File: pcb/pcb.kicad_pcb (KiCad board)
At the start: 2 copper layers, 157 x 88.8 mm, 122 parts, among them J301 USB_C_Receptacle_USB2.0_16P, J302 JTAG, J501 UART, Q201 IRL540N, Q301 Q_Dual_PMOS_S1G1S2G2D2D2D1D1, SW501 Reset, SW502 Boot, T201 DA2032-AL, U1 K155ID1, U2 K155ID1, U201 LM5155, U3 K155ID1, U301 CYPD3176, U4 K155ID1, U401 AP63205WU, U411 AP63203WU, U501 ESP32-S3-WROOM-1

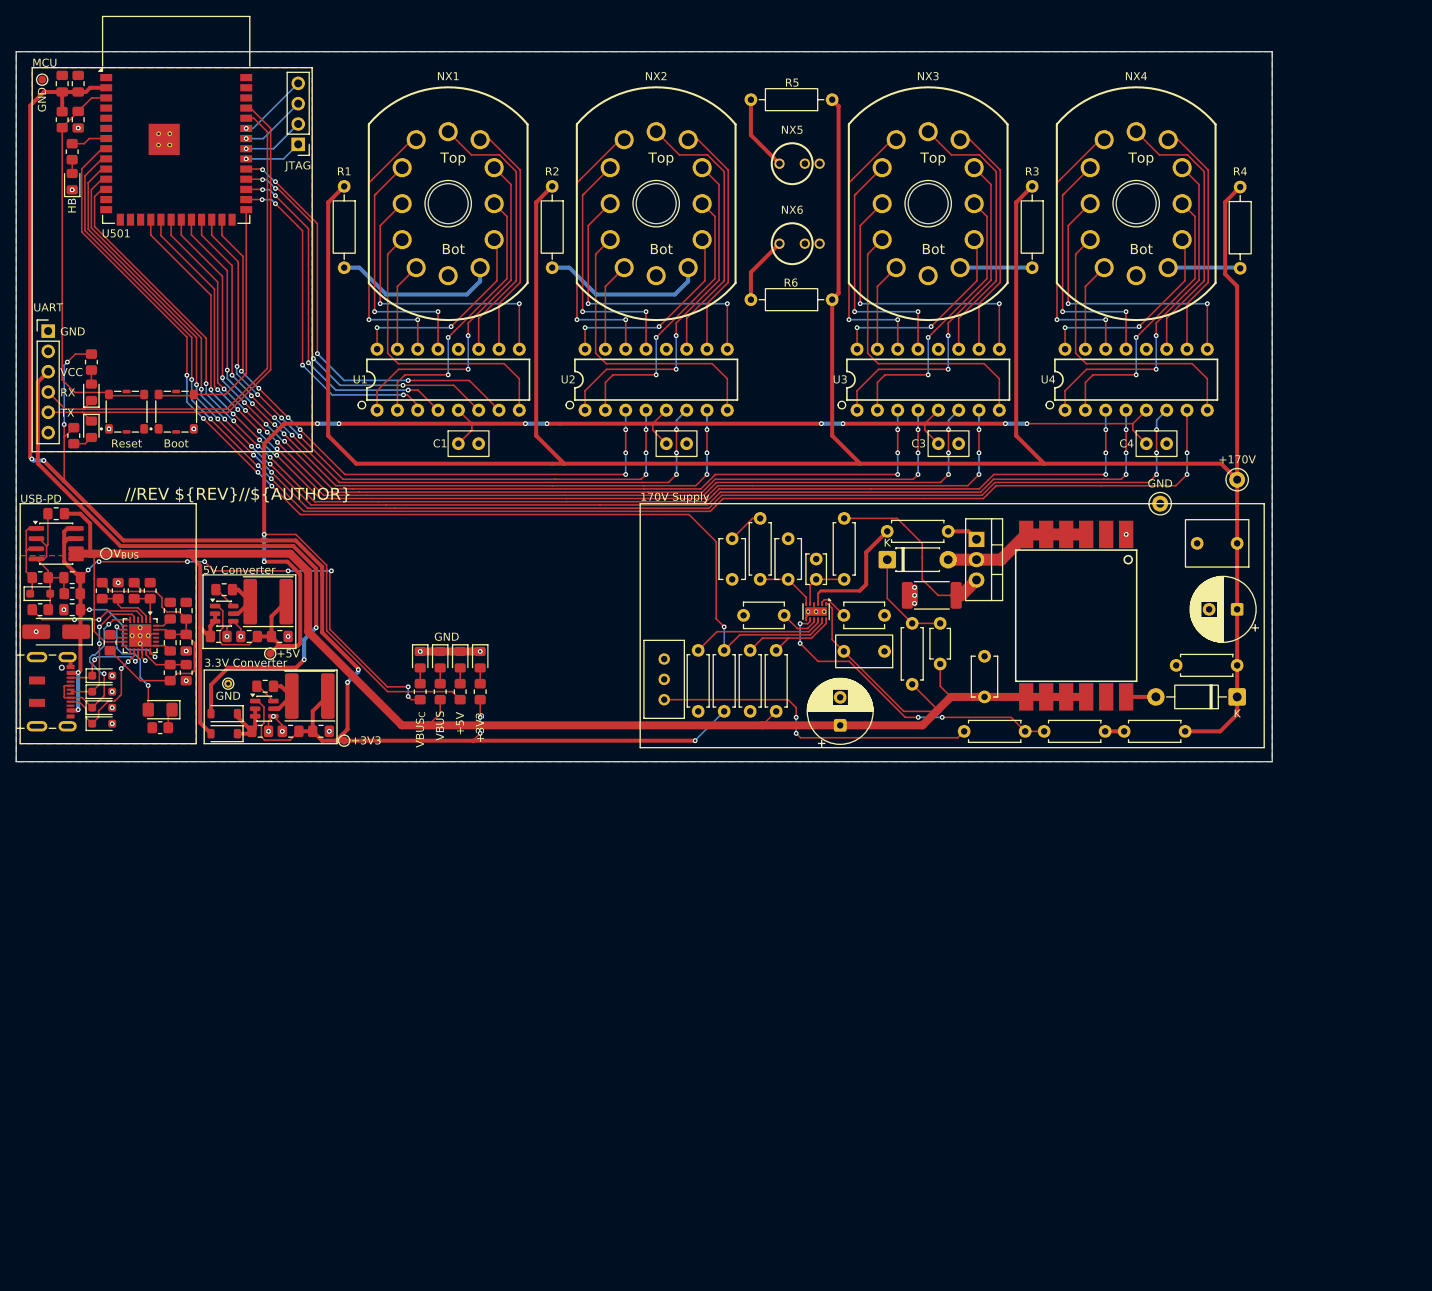
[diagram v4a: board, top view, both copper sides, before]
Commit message: Partial Rev B, committing before splitting projects
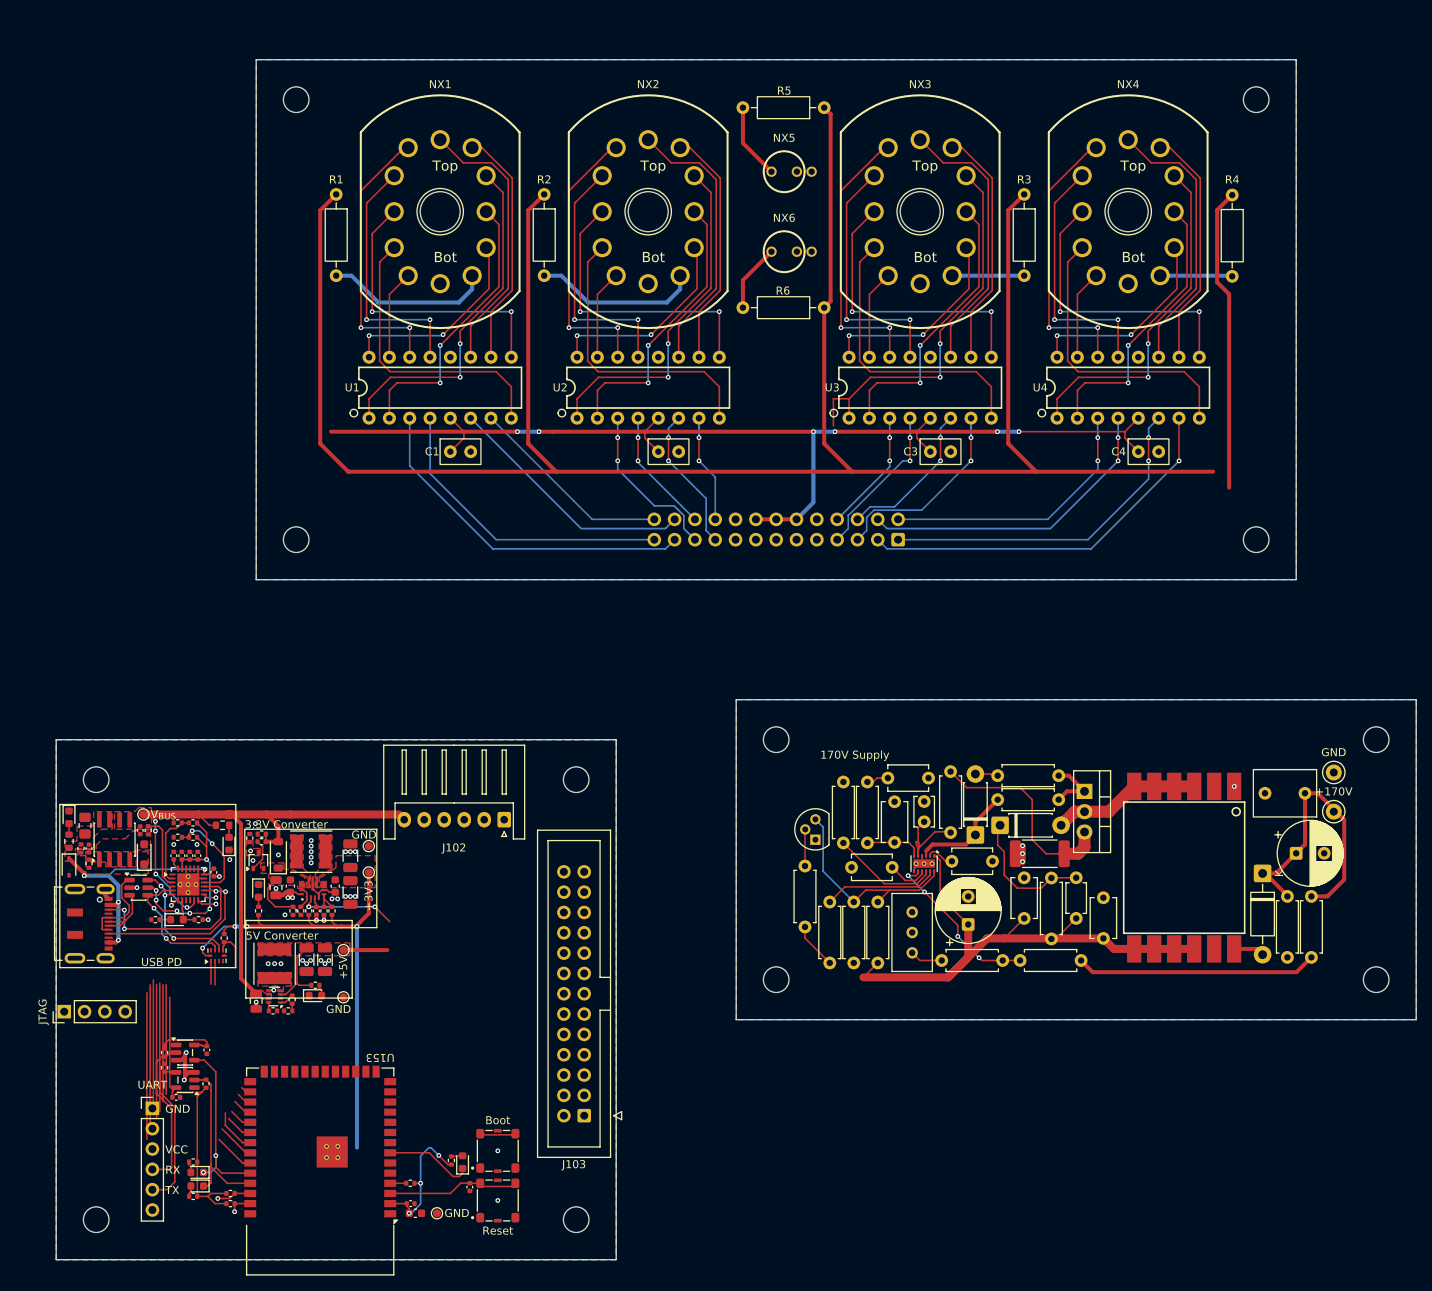
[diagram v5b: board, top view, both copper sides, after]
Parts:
- removed C211: 1uF, nixie_clock:C_Rect_L7.1mm_W4.1mm_P5.08mm_Goldmax
- removed C302, C303, C306, C503: 1uF, Capacitor_SMD:C_0805_2012Metric_Pad1.18x1.45mm_HandSolder
- removed C307, C402, C412: 100nF, Capacitor_SMD:C_0805_2012Metric_Pad1.18x1.45mm_HandSolder
- removed C401, C411: 10uF, Capacitor_SMD:C_0805_2012Metric_Pad1.18x1.45mm_HandSolder
- removed C403, C404, C413, C414: 22uF, Capacitor_SMD:C_0805_2012Metric_Pad1.18x1.45mm_HandSolder
- removed D301: VBUS_{C}, LED_SMD:LED_0805_2012Metric_Pad1.15x1.40mm_HandSolder
- removed D302, D303: ESDA051, Diode_SMD:D_SOD-323_HandSoldering
- removed D304, D306: ESDA051-1JY, Diode_SMD:D_SOD-323_HandSoldering
- removed D309: VBUS, LED_SMD:LED_0805_2012Metric_Pad1.15x1.40mm_HandSolder
- removed D310: HB, LED_SMD:LED_0805_2012Metric_Pad1.15x1.40mm_HandSolder
- removed D401: +5V, LED_SMD:LED_0805_2012Metric_Pad1.15x1.40mm_HandSolder
- removed D411, D412: D_Schottky, Diode_SMD:D_SOD-123
- removed D413: +3V3, LED_SMD:LED_0805_2012Metric_Pad1.15x1.40mm_HandSolder
- removed D501: TX, LED_SMD:LED_0805_2012Metric_Pad1.15x1.40mm_HandSolder
- removed D502: RX, LED_SMD:LED_0805_2012Metric_Pad1.15x1.40mm_HandSolder
- removed L401, L411: 4.7uH, Inductor_SMD:L_APV_ANR6045
- removed R301, R303, R307, R309, R401: 5.1k, Resistor_SMD:R_0805_2012Metric_Pad1.20x1.40mm_HandSolder
- removed R302, R312, R501: 10k, Resistor_SMD:R_0805_2012Metric_Pad1.20x1.40mm_HandSolder
- removed R304, R306, R310, R313: 1k, Resistor_SMD:R_0805_2012Metric_Pad1.20x1.40mm_HandSolder
- removed R314, R411, R502, R503: 1.5k, Resistor_SMD:R_0805_2012Metric_Pad1.20x1.40mm_HandSolder
- removed TP401: +5V, TestPoint:TestPoint_Pad_D1.0mm
- removed TP402: GND, TestPoint:TestPoint_THTPad_D1.0mm_Drill0.5mm
- removed TP411: +3V3, TestPoint:TestPoint_Pad_D1.0mm
- removed U401: AP63205WU, Package_TO_SOT_SMD:TSOT-23-6
- removed U411: AP63203WU, Package_TO_SOT_SMD:TSOT-23-6
- added C102: 100nF, Capacitor_SMD:C_0402_1005Metric, F.Cu at (49.7, 141.6)
- added C103: 1uF, Capacitor_SMD:C_0402_1005Metric, F.Cu at (44.7, 139.5)
- added C104: 1uF, Capacitor_SMD:C_0402_1005Metric, F.Cu at (34.1, 138.6)
- added C107: 1uF, Capacitor_SMD:C_0402_1005Metric, F.Cu at (40.5, 136.3)
- added C108: 100nF, Capacitor_SMD:C_0402_1005Metric, F.Cu at (47.7, 139.5)
- added C109: 10nF, nixie_clock:C_Rect_L5.1mm_W3.2mm_P5.08mm_Goldmax, F.Cu at (151.0, 144.8)
- added C121: 10uF, Capacitor_SMD:C_0805_2012Metric, F.Cu at (57.5, 143.5)
- added C122: 10uF, Capacitor_SMD:C_0603_1608Metric, F.Cu at (59.3, 143.3)
- added C123: 100nF, Capacitor_SMD:C_0402_1005Metric, F.Cu at (62.5, 146.4)
- added C124: 10uF, Capacitor_SMD:C_0603_1608Metric, F.Cu at (64.9, 143.3)
- added C125: 22uF, Capacitor_SMD:C_1206_3216Metric, F.Cu at (66.8, 144.1)
- added C126: 47uF, Capacitor_SMD:C_1206_3216Metric, F.Cu at (66.8, 139.5)
- added C131: 10uF, Capacitor_SMD:C_0805_2012Metric, F.Cu at (55.0, 157.7)
- added C132: 22uF, Capacitor_SMD:C_1206_3216Metric, F.Cu at (61.3, 152.5)
- added C133: 22uF, Capacitor_SMD:C_1206_3216Metric, F.Cu at (63.6, 152.5)
- added C151: 100nF, Capacitor_SMD:C_0402_1005Metric, F.Cu at (45.0, 169.7)
- added C152: 100nF, Capacitor_SMD:C_0402_1005Metric, F.Cu at (48.8, 163.8)
- added C153: 100nF, Capacitor_SMD:C_0402_1005Metric, F.Cu at (81.7, 180.9)
- added D1: SB240S, Diode_THT:D_DO-41_SOD81_P7.62mm_Horizontal, F.Cu at (144.9, 136.9)
- added D101: V_{BUSC}, LED_SMD:LED_0603_1608Metric, F.Cu at (31.6, 134.7)
- added D105: V_{BUS}, LED_SMD:LED_0603_1608Metric, F.Cu at (51.6, 138.0)
- added D121: 1N5819, Diode_SMD:D_SOD-123, F.Cu at (57.8, 139.4)
- added D122: +3.3V, LED_SMD:LED_0603_1608Metric, F.Cu at (55.3, 143.9)
- added D131: +5V, LED_SMD:LED_0603_1608Metric, F.Cu at (62.4, 157.0)
- added D151: TX, LED_SMD:LED_0603_1608Metric, F.Cu at (47.6, 180.8)
- added D152: RX, LED_SMD:LED_0603_1608Metric, F.Cu at (47.6, 179.1)
- added D153: HB, LED_SMD:LED_0603_1608Metric, F.Cu at (80.8, 177.8)
- added H101: MountingHole, MountingHole:MountingHole_3.2mm_M3_ISO7380, F.Cu at (35.0, 130.0)
- added H102: MountingHole, MountingHole:MountingHole_3.2mm_M3_ISO7380, F.Cu at (95.0, 130.0)
- added H103: MountingHole, MountingHole:MountingHole_3.2mm_M3_ISO7380, F.Cu at (35.0, 185.0)
- added H104: MountingHole, MountingHole:MountingHole_3.2mm_M3_ISO7380, F.Cu at (95.0, 185.0)
- added H2: MountingHole, MountingHole:MountingHole_3.2mm_M3_ISO7380, F.Cu at (60.0, 45.0)
- added H3: MountingHole, MountingHole:MountingHole_3.2mm_M3_ISO7380, F.Cu at (180.0, 45.0)
- added H4: MountingHole, MountingHole:MountingHole_3.2mm_M3_ISO7380, F.Cu at (60.0, 100.0)
- added H5: MountingHole, MountingHole:MountingHole_3.2mm_M3_ISO7380, F.Cu at (180.0, 100.0)
- added H6: MountingHole, MountingHole:MountingHole_3.2mm_M3_ISO7380, F.Cu at (120.0, 125.0)
- added H7: MountingHole, MountingHole:MountingHole_3.2mm_M3_ISO7380, F.Cu at (195.0, 125.0)
- added H8: MountingHole, MountingHole:MountingHole_3.2mm_M3_ISO7380, F.Cu at (120.0, 155.0)
- added H9: MountingHole, MountingHole:MountingHole_3.2mm_M3_ISO7380, F.Cu at (195.0, 155.0)
- added J102: Conn_01x06, Connector_JST:JST_XH_S6B-XH-A_1x06_P2.50mm_Horizontal, F.Cu at (86.0, 135.0)
- added J103: Conn_02x13_Counter_Clockwise, Connector_IDC:IDC-Header_2x13_P2.54mm_Vertical, F.Cu at (96.0, 172.0)
- added J104: Conn_02x13_Counter_Clockwise, Connector_IDC:IDC-Header_2x13_P2.54mm_Vertical, B.Cu at (135.2, 100.0)
- added L121: 1.5uH, nixie_clock:L_Bourns_SRN5040TA, F.Cu at (61.9, 139.0)
- added L131: 2.2uH, nixie_clock:L_Bourns_SRN5040TA, F.Cu at (57.3, 153.0)
- added Q121: PMF170XP, Package_TO_SOT_SMD:SOT-323_SC-70, F.Cu at (55.3, 140.1)
- added Q151: TN2106N3-G, Package_TO_SOT_THT:TO-92L, F.Cu at (124.9, 137.5)
- added R101: 5.1k, Resistor_SMD:R_0603_1608Metric, F.Cu at (31.6, 137.7)
- added R102: 10k, Resistor_SMD:R_0402_1005Metric, F.Cu at (51.0, 149.8)
- added R103: 10k, Resistor_SMD:R_0402_1005Metric, F.Cu at (33.1, 138.6)
- added R105: 1k, Resistor_SMD:R_0402_1005Metric, F.Cu at (41.5, 136.3)
- added R106: 5.1k, Resistor_SMD:R_0402_1005Metric, F.Cu at (47.1, 137.2)
- added R107: 2.4k, Resistor_SMD:R_0402_1005Metric, F.Cu at (45.2, 137.2)
- added R108: 5.1k, Resistor_SMD:R_0402_1005Metric, F.Cu at (47.1, 135.4)
- added R111: 5.1k, Resistor_SMD:R_0603_1608Metric, F.Cu at (50.8, 135.7)
- added R112: 100k, Resistor_SMD:R_0402_1005Metric, F.Cu at (47.8, 147.5)
- added R113: 10k, Resistor_SMD:R_0402_1005Metric, F.Cu at (55.7, 136.8)
- added R121: 10k, Resistor_SMD:R_0402_1005Metric, F.Cu at (59.6, 146.4)
- added R122: 100k, Resistor_SMD:R_0402_1005Metric, F.Cu at (55.7, 137.8)
- added R123: 100k, Resistor_SMD:R_0402_1005Metric, F.Cu at (54.2, 137.3)
- added R124: 10k, Resistor_SMD:R_0402_1005Metric, F.Cu at (60.6, 146.4)
- added R125: 120k, Resistor_SMD:R_0402_1005Metric, F.Cu at (64.5, 146.4)
- added R126: 39k, Resistor_SMD:R_0402_1005Metric, F.Cu at (63.5, 146.4)
- added R127: 100k, Resistor_SMD:R_0402_1005Metric, F.Cu at (61.6, 146.4)
- added R128: 1k, Resistor_SMD:R_0402_1005Metric, F.Cu at (55.3, 146.4)
- added R13: 3.3, Resistor_THT:R_Axial_DIN0207_L6.3mm_D2.5mm_P7.62mm_Horizontal, F.Cu at (147.7, 129.5)
- added R131: 27k, Resistor_SMD:R_0402_1005Metric, F.Cu at (57.1, 158.9)
- added R132: 75k, Resistor_SMD:R_0402_1005Metric, F.Cu at (59.5, 157.5)
- added R133: 5.6k, Resistor_SMD:R_0402_1005Metric, F.Cu at (59.0, 158.9)
- added R134: 2.2k, Resistor_SMD:R_0402_1005Metric, F.Cu at (62.4, 155.7)
- added R151: 150, Resistor_SMD:R_0402_1005Metric, F.Cu at (43.6, 166.0)
- added R152: 10k, Resistor_SMD:R_0402_1005Metric, F.Cu at (43.6, 164.1)
- added R153: 680, Resistor_SMD:R_0402_1005Metric, F.Cu at (47.1, 182.1)
- added R154: 680, Resistor_SMD:R_0402_1005Metric, F.Cu at (47.1, 177.8)
- added R155: 10k, Resistor_SMD:R_0402_1005Metric, F.Cu at (48.7, 168.0)
- added R156: 10k, Resistor_SMD:R_0402_1005Metric, F.Cu at (51.8, 183.0)
- added R157: 680, Resistor_SMD:R_0402_1005Metric, F.Cu at (79.4, 177.6)
- added R158: 10k, Resistor_SMD:R_0402_1005Metric, F.Cu at (51.8, 181.7)
- added R159: 10k, Resistor_SMD:R_0402_1005Metric, F.Cu at (74.3, 180.4)
- added R160: 100k, Resistor_THT:R_Axial_DIN0207_L6.3mm_D2.5mm_P7.62mm_Horizontal, F.Cu at (123.6, 148.4)
- added TP121: +3V3, TestPoint:TestPoint_Pad_D1.0mm, F.Cu at (69.1, 141.6)
- added TP122: GND, TestPoint:TestPoint_Pad_D1.0mm, F.Cu at (69.1, 138.3)
- added TP131: +5V, TestPoint:TestPoint_Pad_D1.0mm, F.Cu at (65.9, 151.3)
- added TP132: GND, TestPoint:TestPoint_Pad_D1.0mm, F.Cu at (65.9, 157.2)
- added U101: USBLC6-2SC6, Package_TO_SOT_SMD:SOT-23-6, F.Cu at (40.3, 143.5)
- added U102: TS3USB221A, nixie_clock:UQFN-10_1.5x2mm_P0.5mm_TI_RSE0010A, F.Cu at (50.1, 152.0)
- added U121: TPS63070, nixie_clock:VQFN-15_2.5x3mm_TI_RNM0015A, F.Cu at (62.1, 143.6)
- added U131: TPS629203, Package_TO_SOT_SMD:SOT-583-8, F.Cu at (57.3, 157.1)
- added U151: 74LVC1G17, Package_TO_SOT_SMD:SOT-23-5, F.Cu at (46.1, 167.5)
- added U152: 74LVC1G17, Package_TO_SOT_SMD:SOT-23-5, F.Cu at (46.1, 164.1)
- C105: renamed from C304; footprint Capacitor_SMD:C_0805_2012Metric_Pad1.18x1.45mm_HandSolder -> Capacitor_SMD:C_0402_1005Metric
- C106: renamed from C305; footprint Capacitor_SMD:C_0805_2012Metric_Pad1.18x1.45mm_HandSolder -> Capacitor_SMD:C_0402_1005Metric
- C13: renamed from C209; value 10nF -> 12nF
- C154: renamed from C502; footprint Capacitor_SMD:C_0805_2012Metric_Pad1.18x1.45mm_HandSolder -> Capacitor_SMD:C_0603_1608Metric
- C155: renamed from C501; footprint Capacitor_SMD:C_0805_2012Metric_Pad1.18x1.45mm_HandSolder -> Capacitor_SMD:C_0402_1005Metric
- C9: renamed from C206; value 47nF -> 220nF
- D102: renamed from D305; value SMAJ15A -> SD15Q-7; footprint Diode_SMD:D_SMA_Handsoldering -> Diode_SMD:D_SOD-323
- D104: renamed from D308; footprint LED_SMD:LED_1206_3216Metric_Pad1.42x1.75mm_HandSolder -> LED_SMD:LED_0603_1608Metric
- R104: renamed from R305; footprint Resistor_SMD:R_0805_2012Metric_Pad1.20x1.40mm_HandSolder -> Resistor_SMD:R_0402_1005Metric
- R109: renamed from R308; footprint Resistor_SMD:R_0805_2012Metric_Pad1.20x1.40mm_HandSolder -> Resistor_SMD:R_0402_1005Metric
- R110: renamed from R311; value 220 -> 1k; footprint Resistor_SMD:R_0805_2012Metric_Pad1.20x1.40mm_HandSolder -> Resistor_SMD:R_0402_1005Metric
- R12: renamed from R212; value 27k -> 30k
- R20: renamed from R202; value 470k -> 1.5M
- U5: renamed from U201; footprint Package_SON:WSON-12-1EP_3x2mm_P0.5mm_EP1x2.65_ThermalVias -> nixie_clock:WSON-12-1EP_3x2mm_P0.5mm_EP1x2.65_ThermalVias
- moved TP151 150.0 mm to (77.6, 184.2), turned to 90 degrees
- moved C154 147.9 mm to (74.9, 184.2), turned to 0 degrees
- moved C155 146.0 mm to (74.3, 183.0), turned to 0 degrees
- moved U153 132.7 mm to (63.0, 179.0), turned to 180 degrees
- moved J152 112.3 mm to (31.0, 159.0), turned to 90 degrees
- moved SW152 109.0 mm to (85.2, 182.6)
- moved SW151 100.8 mm to (85.2, 176.4)
- moved J151 98.0 mm to (42.0, 171.1)
- moved RV1 44.3 mm to (137.0, 151.6)
- moved TP2 43.2 mm to (189.7, 134.0)
- moved TP1 40.0 mm to (189.7, 129.1)
- moved Q101 37.7 mm to (37.3, 137.5), turned to 90 degrees
- moved R12 36.3 mm to (154.4, 149.9)
- moved R14 36.3 mm to (147.7, 132.5)
- moved R104 36.3 mm to (34.1, 140.5), turned to 90 degrees
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- renumbered C207 to C10, C301 to C101, C210 to C11, C208 to C12, C204 to C14, C205 to C15, C202 to C5, C203 to C6, C201 to C7, D307 to D103, D202 to D2, D201 to D3, J301 to J101, J501 to J151, J302 to J152, Q201 to Q1, Q301 to Q101, R209 to R10, R210 to R11, R211 to R14, R213 to R15, R201 to R16, R203 to R17, R204 to R18, R205 to R19, R206 to R7, R207 to R8, R208 to R9, RV201 to RV1, SW502 to SW151, SW501 to SW152, T201 to T1, TP202 to TP1, TP301 to TP101, TP501 to TP151, TP201 to TP2, U301 to U103, U501 to U153
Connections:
- net /HV/GATE renamed /HV/GATE_{LM5155}
- net /MCU/EN renamed EN_{MCU}
- net Net-(Q201-G) renamed /HV/GATE_{IRL540N}
- net Net-(Q201-S) renamed /HV/SOURCE_{IRL540N}
- D104 pad 2: /PWR/FAULT -> PD_{FLT}
- J101 pad A6: USB_{D+} -> /PWR/D+_{J}
- J101 pad A7: USB_{D-} -> /PWR/D-_{J}
- J101 pad B6: USB_{D+} -> /PWR/D+_{J}
- J101 pad B7: USB_{D-} -> /PWR/D-_{J}
- J151 pad 4: /MCU/RXD0 -> /MCU/RXD0_{B}
- J151 pad 5: /MCU/TXD0 -> /MCU/TXD0_{B1}
- U103 pad 1: Net-(U301-VBUS_MIN) -> GND
- U103 pad 10: Net-(U301-DATAMODE/FLIP) -> unconnected-(U103-DATAMODE/FLIP-Pad10)
- U103 pad 12: unconnected-(U301-HPI_SDA-Pad12) -> SDA
- U103 pad 13: unconnected-(U301-HPI_SCL-Pad13) -> SCL
- U103 pad 16: GND -> Net-(U103-ISNK_FINE)
- U103 pad 17: Net-(U301-ISNK_COARSE) -> GND
- U103 pad 5: USB_{D+} -> D+
- U103 pad 6: USB_{D-} -> D-
- U103 pad 7: unconnected-(U301-HPI_INT-Pad7) -> PD_{INT}
- U103 pad 8: /PWR/FAULT -> PD_{FLT}
- U153 pad 13: unconnected-(U501-USB_D--Pad13) -> USB_{D-}
- U153 pad 14: unconnected-(U501-USB_D+-Pad14) -> USB_{D+}
- U153 pad 17: unconnected-(U501-GPIO9-Pad17) -> EN_{HV}
- U153 pad 38: unconnected-(U501-GPIO2-Pad38) -> SCL
- U153 pad 39: unconnected-(U501-GPIO1-Pad39) -> SDA
- U153 pad 4: unconnected-(U501-GPIO4-Pad4) -> PD_{INT}
- U153 pad 5: unconnected-(U501-GPIO5-Pad5) -> PD_{FLT}
- U153 pad 6: unconnected-(U501-GPIO6-Pad6) -> USB_{~{OE}}
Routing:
- net M1_{C}: track 177.2 -> 48.0 mm, vias 6 -> 1
- net M1_{B}: track 171.5 -> 42.6 mm, vias 7 -> 2
- net M1_{A}: track 159.8 -> 33.9 mm, vias 7 -> 2
- net PGOOD_{LM5155}: track 140.2 -> 14.4 mm, vias 5 -> 0
- net M1_{D}: track 164.7 -> 39.4 mm, vias 7 -> 2
- net M10_{B}: track 130.8 -> 19.3 mm, vias 7 -> 2
- net M10_{C}: track 135.4 -> 24.6 mm, vias 7 -> 2
- net M10_{A}: track 121.0 -> 15.4 mm, vias 7 -> 2
- net M10_{D}: track 124.9 -> 19.5 mm, vias 7 -> 2
- net +3V3: track 220.6 -> 123.8 mm, vias 9 -> 7
- net H1_{C}: track 95.9 -> 13.5 mm, vias 7 -> 2
- net VCC_{UART}: track 80.8 -> 0.00 mm, vias 2 -> 1
- net V_{BUS}: track 231.3 -> 153.1 mm, vias 0 -> 4
- net H1_{B}: track 91.2 -> 18.1 mm, vias 7 -> 2
- net H1_{D}: track 85.6 -> 15.6 mm, vias 7 -> 2
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- added copper zone on F.Cu, net +3V3
- added copper zone on F.Cu, net +5V
- added copper zone on F.Cu, net /HV/GATE_{LM5155}
- added copper zone on F.Cu, net /PWR/GATE
- added copper zone on F.Cu, net /PWR/L1_{3.3V}
- added copper zone on F.Cu, net /PWR/L2_{3.3V}
- added copper zone on F.Cu, net /PWR/SOURCE
- added copper zone on F.Cu, net /PWR/SW_{5V}
- added copper zone on F.Cu, net /PWR/VBUS_{C}
- added copper zone on F.Cu, net /PWR/VIN_{3.3V}
- added copper zone on F.Cu, net VCC_{UART}
- added copper zone on F.Cu, net V_{BUS}
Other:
- board size 157 x 88.8 mm -> 170 x 150 mm
- board text added: "USB PD"
- board text removed: "Antenna"
- board text removed: "MCU"
- board text removed: "USB-PD"
